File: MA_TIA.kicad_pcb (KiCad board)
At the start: 2 copper layers, 52 x 48 mm, 46 parts, among them M3 MountingHole_3.2mm_M3_DIN965_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, U1 TMA0505D, U2 ADA4350, U3 TPS79301-EP, U4 MIC5270

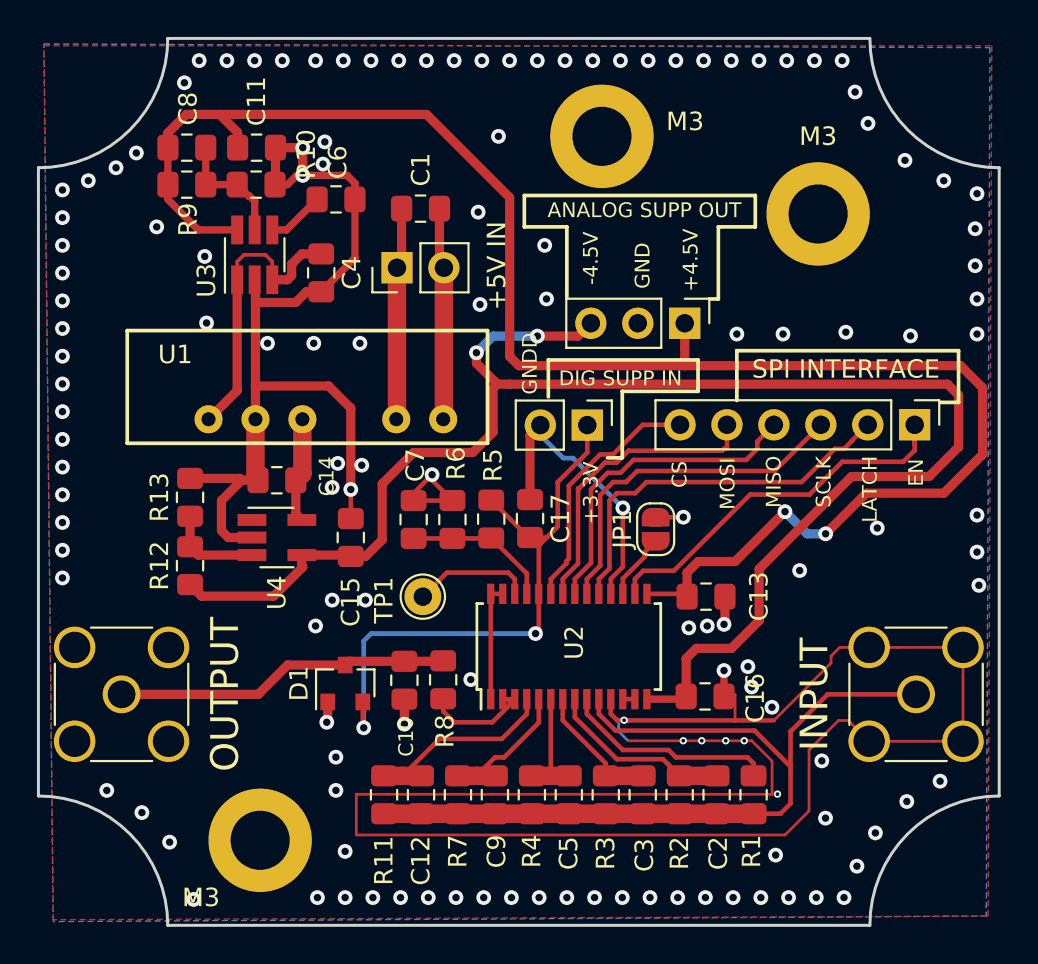
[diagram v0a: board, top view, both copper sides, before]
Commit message: moved two mountig holes slightly inwards
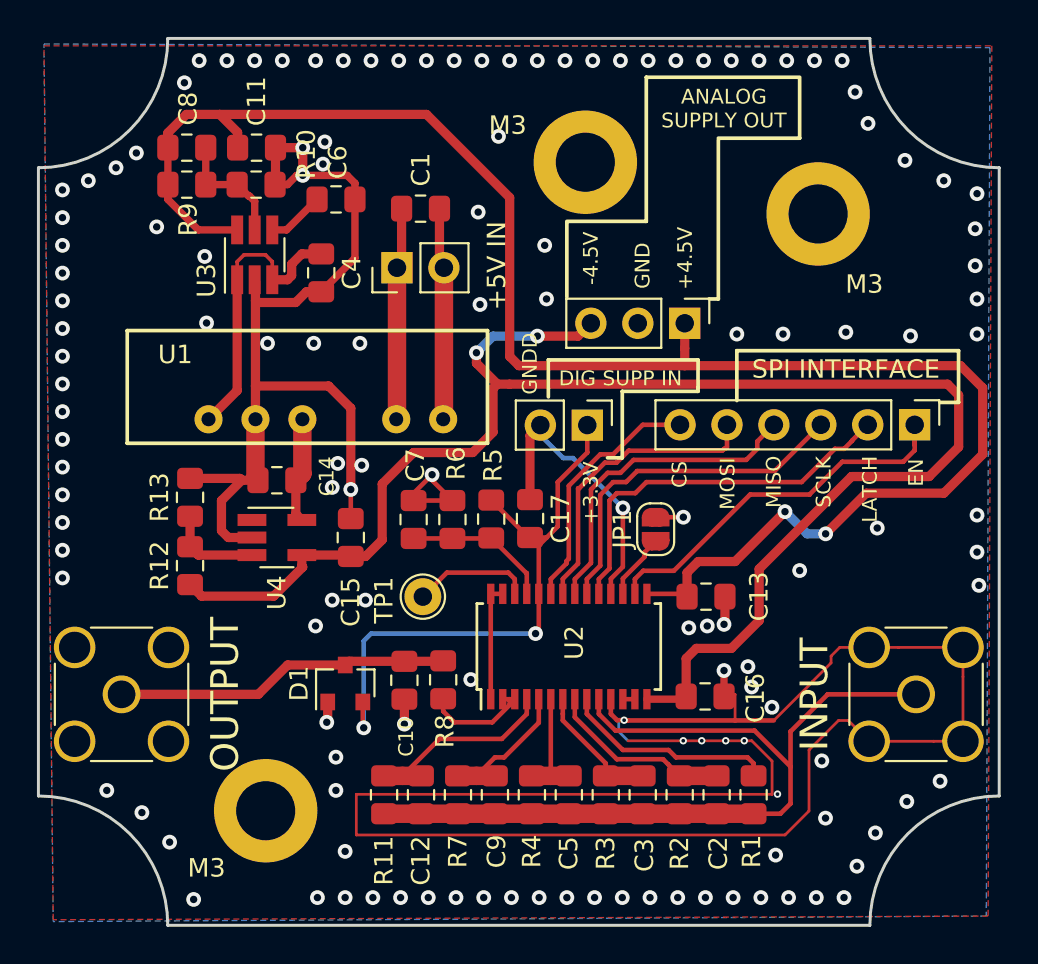
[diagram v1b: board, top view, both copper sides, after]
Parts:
- removed the M3 at (153.0, 79.8)
- removed the M3 at (134.5, 117.9)
- added M3: MountingHole_3.2mm_M3_DIN965_Pad, MountingHole:MountingHole_3.2mm_M3_DIN965_Pad, F.Cu at (152.1, 81.2)
- added M3: MountingHole_3.2mm_M3_DIN965_Pad, MountingHole:MountingHole_3.2mm_M3_DIN965_Pad, F.Cu at (134.8, 116.3)
- +4.5V: renamed from ANALOG SUPP OUT
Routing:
- net Net-(C1-Pad1): vias 1 -> 0
- net GND: vias 134 -> 135
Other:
- board text added: "ANALOG SUPPLY OUT"
- board text removed: "+4.5V"
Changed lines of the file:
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@@
   (page A4)
   (layers
-    (0 F.Cu signal hide)
-    (31 B.Cu signal hide)
+    (0 F.Cu signal)
+    (31 B.Cu signal)
     (32 B.Adhes user)
     (33 F.Adhes user)
@@
   )
   (module MountingHole:MountingHole_3.2mm_M3_DIN965_Pad (layer F.Cu)
-    (at 153 79.8)
+    (at 152.1 81.2)
     (descr "Mounting Hole 3.2mm, M3, DIN965")
     (tags "mounting hole 3.2mm m3 din965")
     (attr virtual)
-    (fp_text reference M3 (at 4.5 -0.8) (layer F.SilkS)
+    (fp_text reference M3 (at -4.2 -2) (layer F.SilkS)
       (effects (font (size 1 1) (thickness 0.15)))
     )
@@
     (tags "mounting hole 3.2mm m3 din965")
     (attr virtual)
-    (fp_text reference M3 (at 0 -4.2) (layer F.SilkS)
+    (fp_text reference M3 (at 2.5 3.8) (layer F.SilkS)
       (effects (font (size 1 1) (thickness 0.15)))
     )
@@
   )
   (module MountingHole:MountingHole_3.2mm_M3_DIN965_Pad (layer F.Cu)
-    (at 134.5 117.9)
+    (at 134.8 116.3)
     (descr "Mounting Hole 3.2mm, M3, DIN965")
     (tags "mounting hole 3.2mm m3 din965")
@@
     (descr "Through hole straight pin header, 1x03, 2.54mm pitch, single row")
     (tags "Through hole pin header THT 1x03 2.54mm single row")
-    (fp_text reference "ANALOG SUPP OUT" (at -6.116 2.18) (layer F.SilkS)
+    (fp_text reference +4.5V (at -3.516 -0.02 90) (layer F.SilkS)
       (effects (font (size 0.8 0.8) (thickness 0.15)))
     )
@@
     )
   )
+  (gr_line (start 163.7 79.9) (end 159.3 79.9) (layer F.SilkS) (width 0.2))
+  (gr_line (start 163.7 76.6) (end 163.7 79.9) (layer F.SilkS) (width 0.2))
+  (gr_line (start 155.4 84.4) (end 155.4 76.6) (layer F.SilkS) (width 0.2))
+  (gr_line (start 151.1 84.4) (end 155.4 84.4) (layer F.SilkS) (width 0.2))
   (gr_line (start 172.3 94.2) (end 171.3 94.2) (layer F.SilkS) (width 0.2))
   (gr_line (start 172.3 91.4) (end 172.3 94.2) (layer F.SilkS) (width 0.2))
@@
   (gr_line (start 160.3 94.1) (end 160.3 91.4) (layer F.SilkS) (width 0.2))
   (gr_line (start 159.3 88.6) (end 158.8 88.6) (layer F.SilkS) (width 0.2))
-  (gr_line (start 159.3 84.7) (end 159.3 88.6) (layer F.SilkS) (width 0.2))
-  (gr_line (start 161.3 84.7) (end 159.3 84.7) (layer F.SilkS) (width 0.2))
-  (gr_line (start 161.3 83) (end 161.3 84.7) (layer F.SilkS) (width 0.2))
-  (gr_line (start 148.8 83) (end 161.3 83) (layer F.SilkS) (width 0.2))
-  (gr_line (start 148.8 84.7) (end 148.8 83) (layer F.SilkS) (width 0.2))
-  (gr_line (start 151.1 84.7) (end 148.8 84.7) (layer F.SilkS) (width 0.2))
-  (gr_line (start 151.1 88.5) (end 151.1 84.7) (layer F.SilkS) (width 0.2))
+  (gr_line (start 159.3 80) (end 159.3 88.6) (layer F.SilkS) (width 0.2))
+  (gr_line (start 155.4 76.6) (end 163.6 76.6) (layer F.SilkS) (width 0.2))
+  (gr_line (start 151.1 88.5) (end 151.1 84.5) (layer F.SilkS) (width 0.2))
   (gr_line (start 154.1 97.2) (end 153.3 97.2) (layer F.SilkS) (width 0.2))
   (gr_line (start 154.1 93.6) (end 154.1 97.2) (layer F.SilkS) (width 0.2))
@@
     (effects (font (size 0.8 0.8) (thickness 0.15)))
   )
-  (gr_text +4.5V (at 157.8 86.5 90) (layer F.SilkS)
+  (gr_text "ANALOG\nSUPPLY OUT" (at 159.6 78.3) (layer F.SilkS)
     (effects (font (size 0.8 0.8) (thickness 0.15)))
   )
@@
   (gr_arc (start 122.5 122.5) (end 129.5 122.5) (angle -90) (layer Edge.Cuts) (width 0.16))
   (gr_arc (start 174.5 122.5) (end 174.5 115.5) (angle -90) (layer Edge.Cuts) (width 0.16))
-  (via (at 123.8 103.7) (size 0.8) (drill 0.4) (layers F.Cu B.Cu) (net 7))
-  (via (at 123.8 102.2) (size 0.8) (drill 0.4) (layers F.Cu B.Cu) (net 7))
-  (via (at 123.8 100.7) (size 0.8) (drill 0.4) (layers F.Cu B.Cu) (net 7))
-  (via (at 123.8 99.2) (size 0.8) (drill 0.4) (layers F.Cu B.Cu) (net 7))
-  (via (at 123.8 97.7) (size 0.8) (drill 0.4) (layers F.Cu B.Cu) (net 7))
-  (via (at 123.8 96.2) (size 0.8) (drill 0.4) (layers F.Cu B.Cu) (net 7))
-  (via (at 123.8 94.7) (size 0.8) (drill 0.4) (layers F.Cu B.Cu) (net 7))
-  (via (at 123.8 93.2) (size 0.8) (drill 0.4) (layers F.Cu B.Cu) (net 7))
-  (via (at 123.8 91.7) (size 0.8) (drill 0.4) (layers F.Cu B.Cu) (net 7))
-  (via (at 123.8 90.2) (size 0.8) (drill 0.4) (layers F.Cu B.Cu) (net 7))
-  (via (at 123.8 88.7) (size 0.8) (drill 0.4) (layers F.Cu B.Cu) (net 7))
-  (via (at 123.8 87.2) (size 0.8) (drill 0.4) (layers F.Cu B.Cu) (net 7))
-  (via (at 123.8 85.7) (size 0.8) (drill 0.4) (layers F.Cu B.Cu) (net 7))
-  (via (at 123.8 84.2) (size 0.8) (drill 0.4) (layers F.Cu B.Cu) (net 7))
-  (via (at 123.8 82.7) (size 0.8) (drill 0.4) (layers F.Cu B.Cu) (net 7))
-  (via (at 130.4 76.9) (size 0.8) (drill 0.4) (layers F.Cu B.Cu) (net 7))
-  (via (at 135.7 75.7) (size 0.8) (drill 0.4) (layers F.Cu B.Cu) (net 7))
-  (via (at 134.2 75.7) (size 0.8) (drill 0.4) (layers F.Cu B.Cu) (net 7))
-  (via (at 132.7 75.7) (size 0.8) (drill 0.4) (layers F.Cu B.Cu) (net 7))
-  (via (at 131.2 75.7) (size 0.8) (drill 0.4) (layers F.Cu B.Cu) (net 7))
-  (via (at 137.6 121) (size 0.8) (drill 0.4) (layers F.Cu B.Cu) (net 7))
   (segment (start 144.446 95.072) (end 144.406 95.112) (width 1) (layer F.Cu) (net 1))
   (segment (start 144.446 86.912) (end 144.446 95.072) (width 1) (layer F.Cu) (net 1))
   (segment (start 144.206 86.672) (end 144.446 86.912) (width 0.5) (layer F.Cu) (net 1))
   (segment (start 144.206 83.712) (end 144.206 86.672) (width 0.5) (layer F.Cu) (net 1))
+  (via (at 149.9 85.7) (size 0.8) (drill 0.4) (layers F.Cu B.Cu) (net 7))
   (segment (start 141.906 95.072) (end 141.866 95.112) (width 1) (layer F.Cu) (net 2))
   (segment (start 141.906 86.912) (end 141.906 95.072) (width 1) (layer F.Cu) (net 2))
@@
   (segment (start 136.756 86.162) (end 137.806 86.162) (width 0.5) (layer F.Cu) (net 6))
   (segment (start 136.206 86.712) (end 136.756 86.162) (width 0.5) (layer F.Cu) (net 6))
+  (via (at 123.8 103.7) (size 0.8) (drill 0.4) (layers F.Cu B.Cu) (net 7))
+  (via (at 123.8 102.2) (size 0.8) (drill 0.4) (layers F.Cu B.Cu) (net 7))
+  (via (at 123.8 100.7) (size 0.8) (drill 0.4) (layers F.Cu B.Cu) (net 7))
+  (via (at 123.8 99.2) (size 0.8) (drill 0.4) (layers F.Cu B.Cu) (net 7))
+  (via (at 123.8 97.7) (size 0.8) (drill 0.4) (layers F.Cu B.Cu) (net 7))
+  (via (at 123.8 96.2) (size 0.8) (drill 0.4) (layers F.Cu B.Cu) (net 7))
+  (via (at 123.8 94.7) (size 0.8) (drill 0.4) (layers F.Cu B.Cu) (net 7))
+  (via (at 123.8 93.2) (size 0.8) (drill 0.4) (layers F.Cu B.Cu) (net 7))
+  (via (at 123.8 91.7) (size 0.8) (drill 0.4) (layers F.Cu B.Cu) (net 7))
+  (via (at 123.8 90.2) (size 0.8) (drill 0.4) (layers F.Cu B.Cu) (net 7))
+  (via (at 123.8 88.7) (size 0.8) (drill 0.4) (layers F.Cu B.Cu) (net 7))
+  (via (at 123.8 87.2) (size 0.8) (drill 0.4) (layers F.Cu B.Cu) (net 7))
+  (via (at 123.8 85.7) (size 0.8) (drill 0.4) (layers F.Cu B.Cu) (net 7))
+  (via (at 123.8 84.2) (size 0.8) (drill 0.4) (layers F.Cu B.Cu) (net 7))
+  (via (at 123.8 82.7) (size 0.8) (drill 0.4) (layers F.Cu B.Cu) (net 7))
+  (via (at 130.4 76.9) (size 0.8) (drill 0.4) (layers F.Cu B.Cu) (net 7))
+  (via (at 135.7 75.7) (size 0.8) (drill 0.4) (layers F.Cu B.Cu) (net 7))
+  (via (at 134.2 75.7) (size 0.8) (drill 0.4) (layers F.Cu B.Cu) (net 7))
+  (via (at 132.7 75.7) (size 0.8) (drill 0.4) (layers F.Cu B.Cu) (net 7))
+  (via (at 131.2 75.7) (size 0.8) (drill 0.4) (layers F.Cu B.Cu) (net 7))
+  (via (at 137.6 121) (size 0.8) (drill 0.4) (layers F.Cu B.Cu) (net 7))
   (via (at 154.2 111.4) (size 0.4) (drill 0.2) (layers F.Cu B.Cu) (net 7))
   (segment (start 154.406 112.512) (end 154.406 112.512) (width 0.15) (layer F.Cu) (net 7))
@@
   (via (at 169.7 90.6) (size 0.8) (drill 0.4) (layers F.Cu B.Cu) (net 7))
   (via (at 150 88.6) (size 0.8) (drill 0.4) (layers F.Cu B.Cu) (net 7))
-  (via (at 149.9 85.7) (size 0.8) (drill 0.4) (layers F.Cu B.Cu) (net 1))
   (via (at 147.4 79.8) (size 0.8) (drill 0.4) (layers F.Cu B.Cu) (net 7))
   (segment (start 150.231 114.387) (end 150.206 114.412) (width 0.25) (layer F.Cu) (net 8))

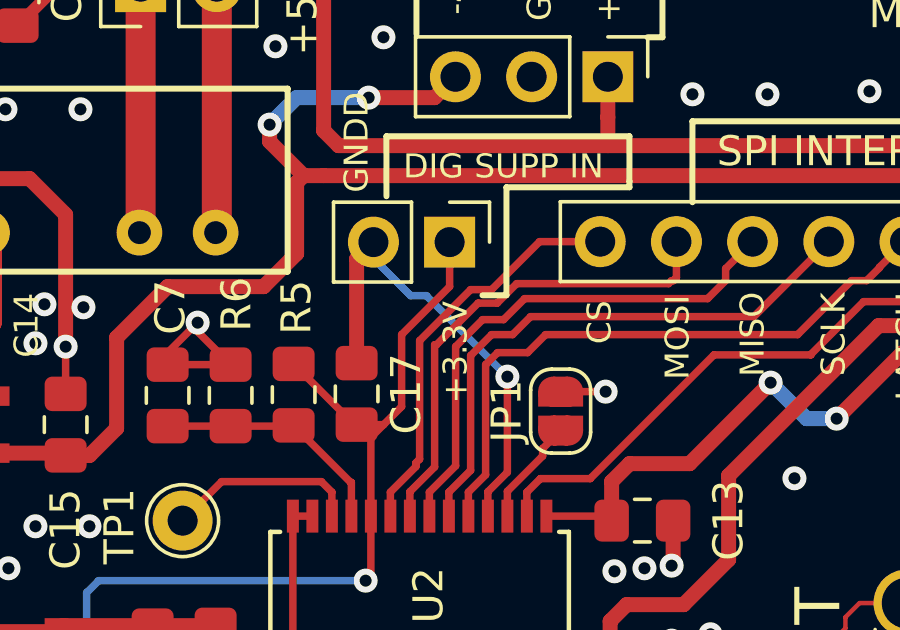
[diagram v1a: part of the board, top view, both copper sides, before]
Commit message: fix: removed separate digital ground
fix: removed separate digital ground (GNDD) and connected it to GND
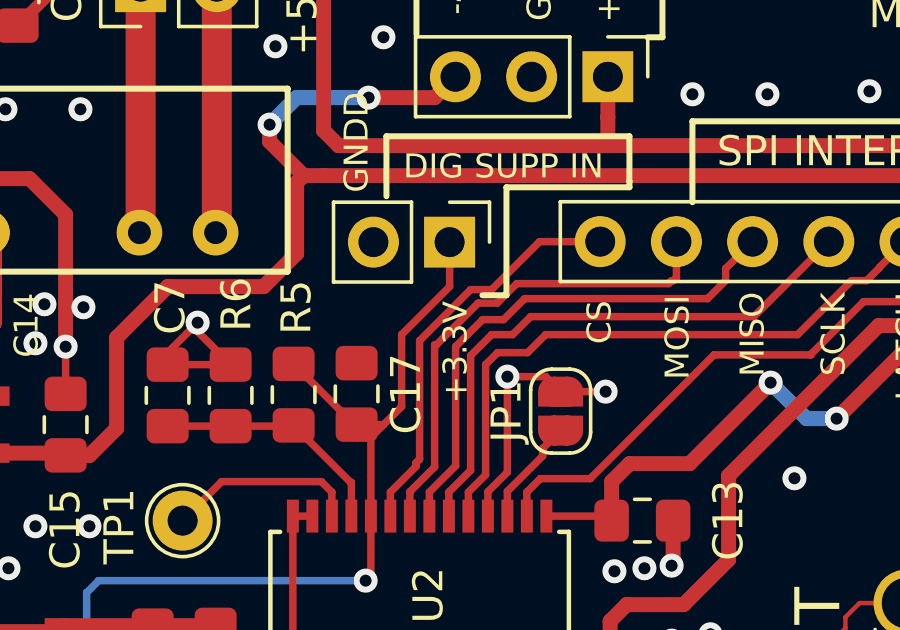
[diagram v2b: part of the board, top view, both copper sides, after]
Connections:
- C17 pad 1: GNDD -> GND
- DIG SUPP IN pad 2: GNDD -> GND
- U2 pad 18: GNDD -> GND
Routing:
- net GNDD: track 15.8 -> 0.00 mm, vias 1 -> 0
- net GND: track 166.9 -> 173.8 mm, vias 135 -> 136
